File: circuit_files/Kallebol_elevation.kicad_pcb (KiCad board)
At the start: 2 copper layers, 86.9 x 80.3 mm, 55 parts, among them IC1 BD62130AEFJ-E2, J1 Home_switch, J10 Conn_01x05_Male, J11 UART/I2C, J2 Encoder, J3 Limit Switch, J4 Power in, J5 power_out, J6 Screw_Terminal_01x02, J7 Screw_Terminal_01x02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

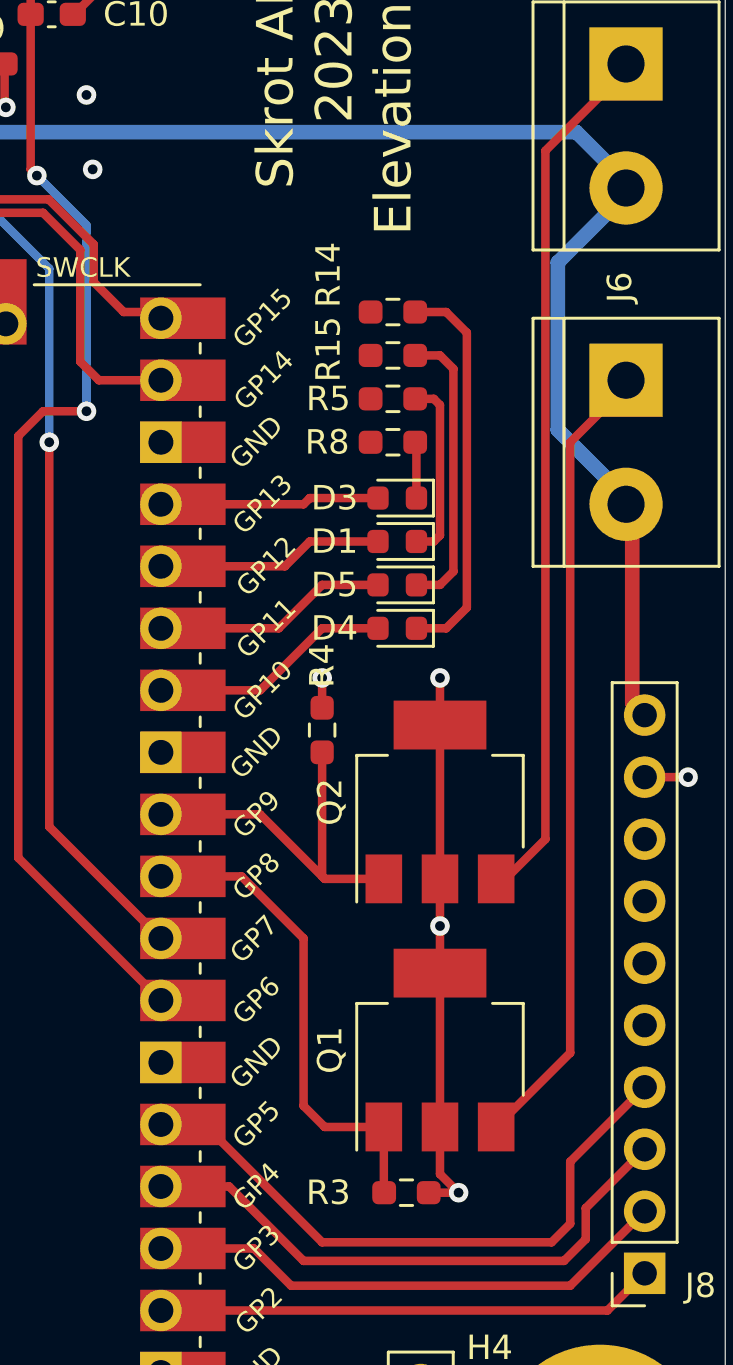
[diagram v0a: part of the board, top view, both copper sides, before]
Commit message: fixed issue with reversed mosfet
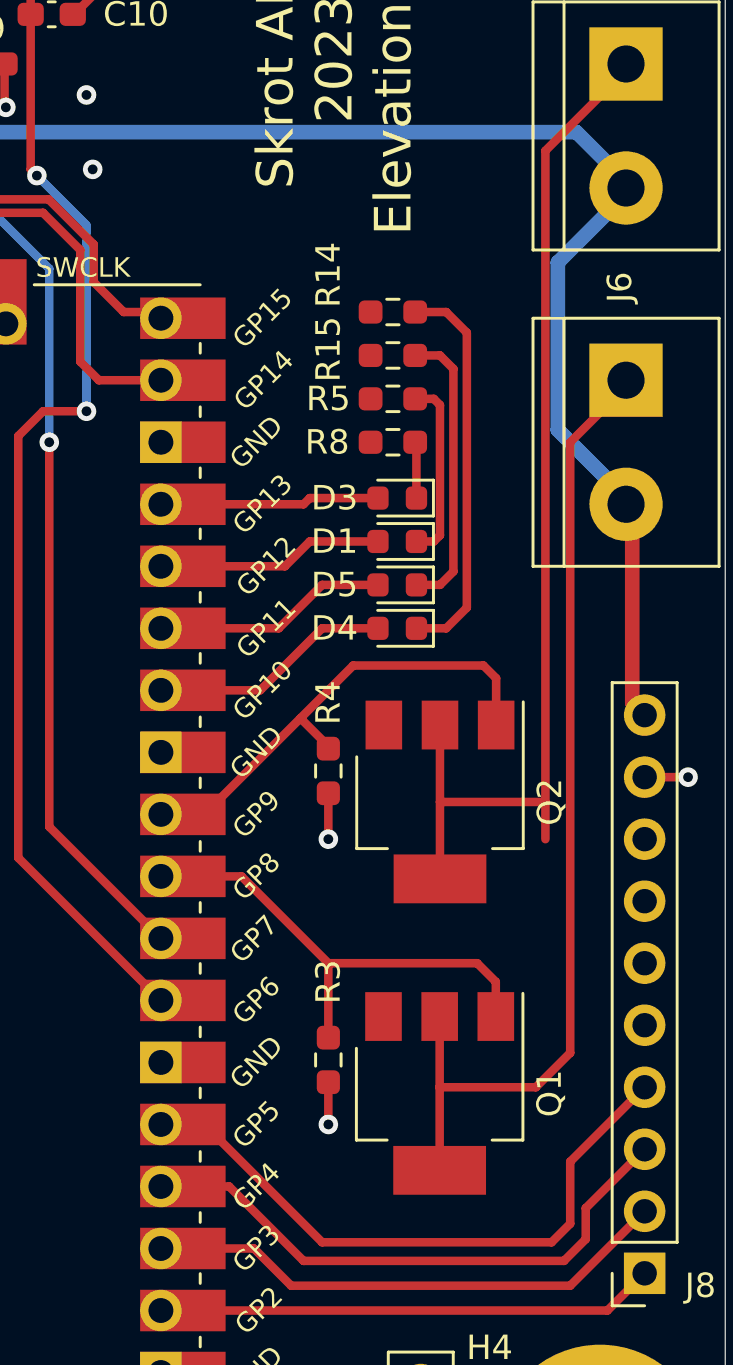
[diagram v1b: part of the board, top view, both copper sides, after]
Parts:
- moved R3 6.31 mm to (118.9, 104.0), turned to -90 degrees
- moved Q1 1.78 mm to (123.4, 105.4), turned to -90 degrees
- moved R4 1.69 mm to (118.9, 92.2), turned to -90 degrees
- turned Q2 to -90 degrees
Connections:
- Q1 pad 2: GND -> Net-(J6-Pin_1)
- Q1 pad 3: Net-(J6-Pin_1) -> GND
- Q2 pad 2: GND -> Net-(J7-Pin_1)
- Q2 pad 3: Net-(J7-Pin_1) -> GND
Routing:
- net GND: track 73.0 -> 52.8 mm, vias 46 -> 44
- net Net-(J6-Pin_1): track 32.9 -> 40.8 mm
- net Net-(J7-Pin_1): track 35.9 -> 43.8 mm
- net Load2_enable: track 15.3 -> 20.1 mm
